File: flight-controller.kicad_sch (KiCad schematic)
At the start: 25 parts, among them CN10 Conn_02x17_Odd_Even, CN7 Conn_02x10_Odd_Even, CN8 Conn_02x08_Odd_Even, CN9 Conn_02x15_Odd_Even, J1 Conn_01x04, J7 J_ESC_POWER, Q1 2N2222

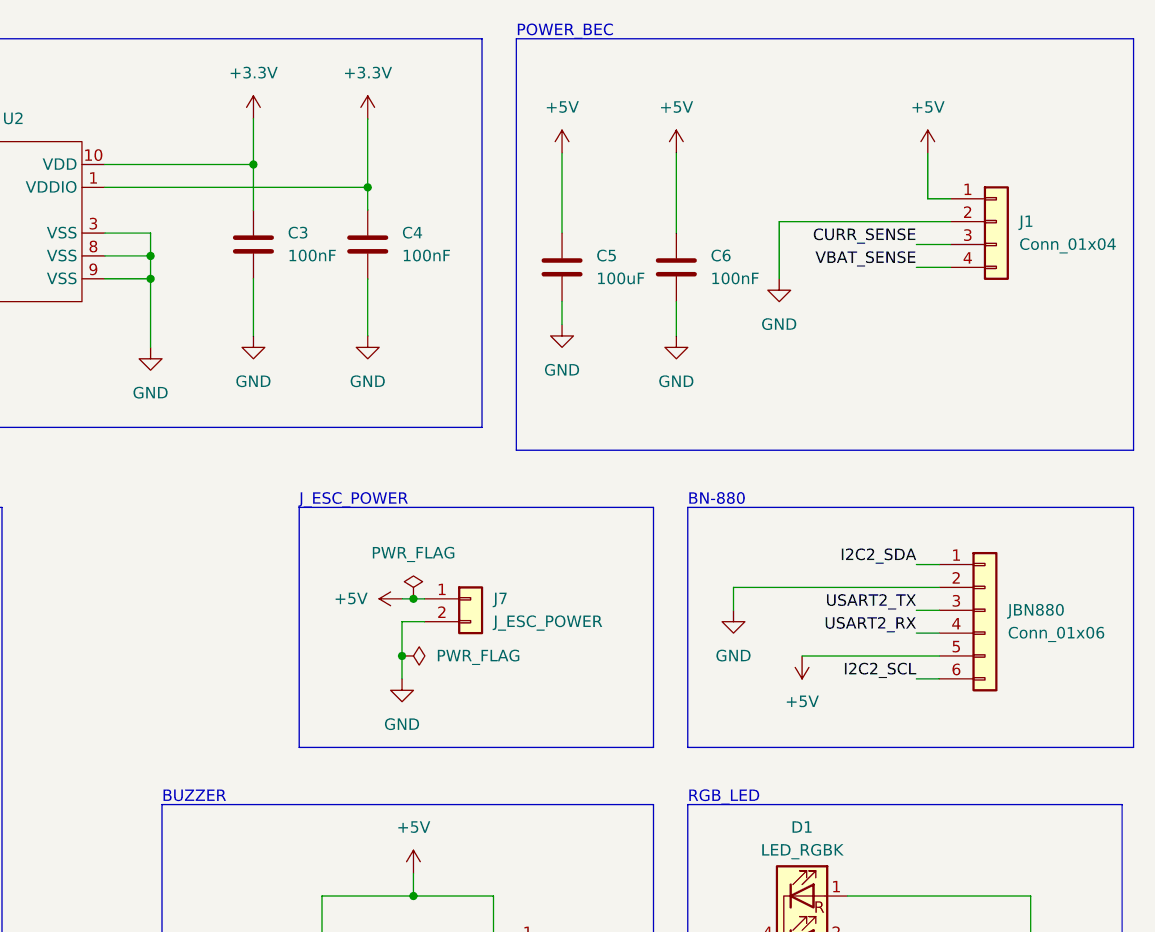
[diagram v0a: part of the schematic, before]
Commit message: feat: Added diodes to power inputs
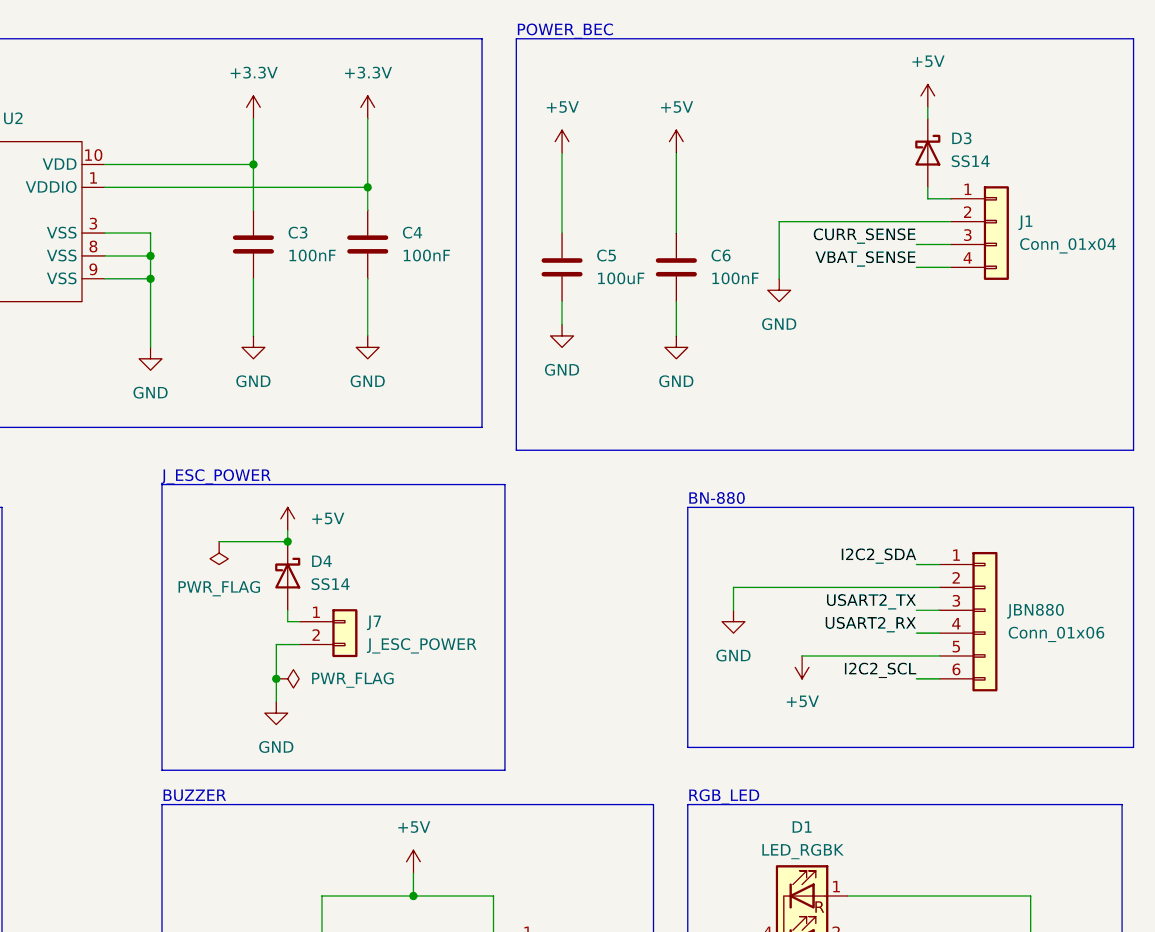
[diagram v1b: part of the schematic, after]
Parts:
- added D3, D4: SS14, symbol Device:D_Schottky
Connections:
- net +5V: now also D3.1 (K), D4.1 (K); no longer J1.1 (Pin_1), J7.1 (Pin_1)
- new net: D4.2 (A), J7.1 (Pin_1)
- new net: D3.2 (A), J1.1 (Pin_1)
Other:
- moved on the sheet: J7

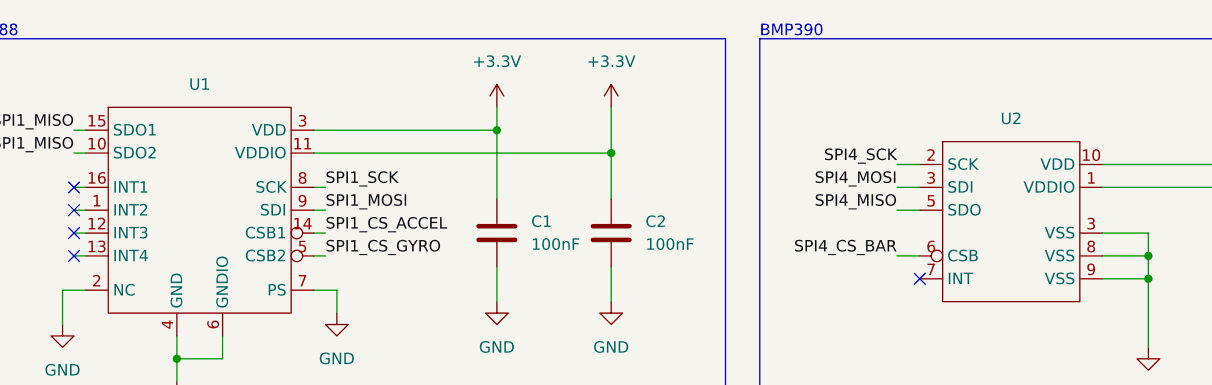
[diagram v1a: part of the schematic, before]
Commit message: fix: Added values to bmi and bmp sensors
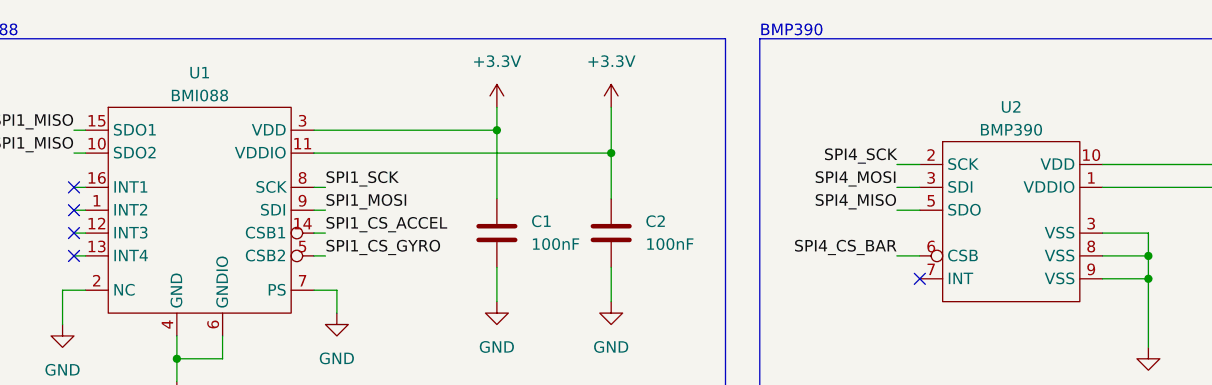
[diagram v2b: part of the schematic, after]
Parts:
- U1: value ~ -> BMI088
- U2: value ~ -> BMP390
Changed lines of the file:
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@@
   )
   (symbol (lib_id "fc_custom:BMI088") (at 48.26 43.18 0) (unit 1)
-    (in_bom yes) (on_board yes) (dnp no) (fields_autoplaced)
-    (property "Reference" "U1" (at 48.26 29.21 0)
-      (effects (font (size 1.27 1.27)))
-    )
-    (property "Value" "~" (at 48.26 43.18 0)
+    (in_bom yes) (on_board yes) (dnp no)
+    (property "Reference" "U1" (at 48.26 27.94 0)
+      (effects (font (size 1.27 1.27)))
+    )
+    (property "Value" "BMI088" (at 48.26 30.48 0)
       (effects (font (size 1.27 1.27)))
     )
@@
   )
   (symbol (lib_id "fc_custom:BMP390") (at 138.43 44.45 0) (unit 1)
-    (in_bom yes) (on_board yes) (dnp no) (fields_autoplaced)
-    (property "Reference" "U2" (at 138.43 33.02 0)
-      (effects (font (size 1.27 1.27)))
-    )
-    (property "Value" "~" (at 138.43 44.45 0)
-      (effects (font (size 1.27 1.27)))
-    )
+    (in_bom yes) (on_board yes) (dnp no)
+    (property "Reference" "U2" (at 138.43 31.75 0)
+      (effects (font (size 1.27 1.27)))
+    )
+    (property "Value" "BMP390" (at 138.43 34.29 0)
+      (effects (font (size 1.27 1.27)))
+    )

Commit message: chore: Added footprints to elements
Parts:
- BZ1: footprint (none) -> Buzzer_Beeper:Buzzer_12x9.5mm_P7.60mm
- C1, C2, C3, C4, C6: footprint (none) -> Capacitor_SMD:C_0402_1005Metric
- C5: footprint (none) -> Capacitor_THT:CP_Radial_D6.3mm_P2.50mm
- CN10: footprint (none) -> Connector_PinHeader_2.54mm:PinHeader_2x17_P2.54mm_Vertical
- CN7: footprint (none) -> Connector_PinHeader_2.54mm:PinHeader_2x10_P2.54mm_Vertical
- CN8: footprint (none) -> Connector_PinHeader_2.54mm:PinHeader_2x08_P2.54mm_Vertical
- CN9: footprint (none) -> Connector_PinHeader_2.54mm:PinHeader_2x15_P2.54mm_Vertical
- D1: footprint (none) -> LED_THT:LED_D5.0mm-4_RGB
- D3, D4: footprint (none) -> Diode_SMD:D_SOD-123
- J1: footprint (none) -> Connector_PinHeader_2.54mm:PinHeader_1x04_P2.54mm_Vertical
- J7: footprint (none) -> Connector_PinHeader_2.54mm:PinHeader_1x02_P2.54mm_Vertical
- JBN880: footprint (none) -> Connector_PinHeader_2.54mm:PinHeader_1x06_P2.54mm_Vertical
- Q1: footprint Package_TO_SOT_THT:TO-39-3 -> Package_TO_SOT_THT:TO-92_Inline
- R1, R2, R3, R4, R5, R6: footprint (none) -> Resistor_SMD:R_0402_1005Metric
- U1: footprint (none) -> fc_library:BMI088
- U2: footprint (none) -> fc_library:BMP390L
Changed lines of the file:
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@@
       (effects (font (size 1.27 1.27)) (justify right))
     )
-    (property "Footprint" "" (at 93.0148 41.91 0)
+    (property "Footprint" "Capacitor_SMD:C_0402_1005Metric" (at 93.0148 41.91 0)
       (effects (font (size 1.27 1.27)) hide)
     )
@@
       (effects (font (size 1.27 1.27)))
     )
-    (property "Footprint" "" (at 63.5 97.79 0)
+    (property "Footprint" "Connector_PinHeader_2.54mm:PinHeader_2x08_P2.54mm_Vertical" (at 63.5 97.79 0)
       (effects (font (size 1.27 1.27)) hide)
     )
@@
       (effects (font (size 1.27 1.27)) (justify left))
     )
-    (property "Footprint" "" (at 242.062 135.89 90)
+    (property "Footprint" "Resistor_SMD:R_0402_1005Metric" (at 242.062 135.89 90)
       (effects (font (size 1.27 1.27)) hide)
     )
@@
       (effects (font (size 1.27 1.27)) (justify left))
     )
-    (property "Footprint" "Package_TO_SOT_THT:TO-39-3" (at 185.42 146.685 0)
+    (property "Footprint" "Package_TO_SOT_THT:TO-92_Inline" (at 185.42 146.685 0)
       (effects (font (size 1.27 1.27) italic) (justify left) hide)
     )
@@
       (effects (font (size 1.27 1.27)))
     )
-    (property "Footprint" "" (at 48.26 43.18 0)
-      (effects (font (size 1.27 1.27)) hide)
-    )
-    (property "Datasheet" "" (at 48.26 43.18 0)
+    (property "Footprint" "fc_library:BMI088" (at 48.26 43.18 0)
+      (effects (font (size 1.27 1.27)) hide)
+    )
+    (property "Datasheet" "https://www.bosch-sensortec.com/media/boschsensortec/downloads/datasheets/bst-bmi088-ds001.pdf" (at 48.26 43.18 0)
       (effects (font (size 1.27 1.27)) hide)
     )
@@
       (effects (font (size 1.27 1.27)) (justify left))
     )
-    (property "Footprint" "" (at 168.91 83.82 0)
+    (property "Footprint" "Diode_SMD:D_SOD-123" (at 168.91 83.82 0)
       (effects (font (size 1.27 1.27)) hide)
     )
@@
       (effects (font (size 1.27 1.27)) (justify left))
     )
-    (property "Footprint" "" (at 40.132 121.92 90)
+    (property "Footprint" "Resistor_SMD:R_0402_1005Metric" (at 40.132 121.92 90)
       (effects (font (size 1.27 1.27)) hide)
     )
@@
       (effects (font (size 1.27 1.27)) (justify left))
     )
-    (property "Footprint" "" (at 35.052 143.51 90)
+    (property "Footprint" "Resistor_SMD:R_0402_1005Metric" (at 35.052 143.51 90)
       (effects (font (size 1.27 1.27)) hide)
     )
@@
       (effects (font (size 1.27 1.27)) (justify left))
     )
-    (property "Footprint" "" (at 246.38 87.63 0)
+    (property "Footprint" "Connector_PinHeader_2.54mm:PinHeader_1x06_P2.54mm_Vertical" (at 246.38 87.63 0)
       (effects (font (size 1.27 1.27)) hide)
     )
@@
       (effects (font (size 1.27 1.27)))
     )
-    (property "Footprint" "" (at 111.76 146.05 0)
+    (property "Footprint" "Connector_PinHeader_2.54mm:PinHeader_2x17_P2.54mm_Vertical" (at 111.76 146.05 0)
       (effects (font (size 1.27 1.27)) hide)
     )
@@
       (effects (font (size 1.27 1.27)) (justify left))
     )
-    (property "Footprint" "" (at 240.03 36.83 0)
+    (property "Footprint" "Diode_SMD:D_SOD-123" (at 240.03 36.83 0)
       (effects (font (size 1.27 1.27)) hide)
     )
@@
       (effects (font (size 1.27 1.27)))
     )
-    (property "Footprint" "" (at 226.06 125.73 0)
+    (property "Footprint" "LED_THT:LED_D5.0mm-4_RGB" (at 226.06 125.73 0)
       (effects (font (size 1.27 1.27)) hide)
     )
@@
       (effects (font (size 1.27 1.27)) (justify left))
     )
-    (property "Footprint" "" (at 200.3552 53.34 0)
+    (property "Footprint" "Capacitor_THT:CP_Radial_D6.3mm_P2.50mm" (at 200.3552 53.34 0)
       (effects (font (size 1.27 1.27)) hide)
     )
@@
       (effects (font (size 1.27 1.27)) (justify left))
     )
-    (property "Footprint" "" (at 247.65 44.45 0)
+    (property "Footprint" "Connector_PinHeader_2.54mm:PinHeader_1x04_P2.54mm_Vertical" (at 247.65 44.45 0)
       (effects (font (size 1.27 1.27)) hide)
     )
@@
       (effects (font (size 1.27 1.27)) (justify left))
     )
-    (property "Footprint" "" (at 82.2452 49.53 0)
+    (property "Footprint" "Capacitor_SMD:C_0402_1005Metric" (at 82.2452 49.53 0)
       (effects (font (size 1.27 1.27)) hide)
     )
@@
       (effects (font (size 1.27 1.27)) (justify left))
     )
-    (property "Footprint" "" (at 213.0552 53.34 0)
+    (property "Footprint" "Capacitor_SMD:C_0402_1005Metric" (at 213.0552 53.34 0)
       (effects (font (size 1.27 1.27)) hide)
     )
@@
       (effects (font (size 1.27 1.27)) (justify left))
     )
-    (property "Footprint" "" (at 234.442 135.89 90)
+    (property "Footprint" "Resistor_SMD:R_0402_1005Metric" (at 234.442 135.89 90)
       (effects (font (size 1.27 1.27)) hide)
     )
@@
       (effects (font (size 1.27 1.27)))
     )
-    (property "Footprint" "" (at 168.91 146.558 90)
+    (property "Footprint" "Resistor_SMD:R_0402_1005Metric" (at 168.91 146.558 90)
       (effects (font (size 1.27 1.27)) hide)
     )
@@
       (effects (font (size 1.27 1.27)) (justify left))
     )
-    (property "Footprint" "" (at 196.215 124.46 90)
+    (property "Footprint" "Buzzer_Beeper:Buzzer_12x9.5mm_P7.60mm" (at 196.215 124.46 90)
       (effects (font (size 1.27 1.27)) hide)
     )
@@
       (effects (font (size 1.27 1.27)) (justify left))
     )
-    (property "Footprint" "" (at 175.26 88.9 0)
+    (property "Footprint" "Connector_PinHeader_2.54mm:PinHeader_1x02_P2.54mm_Vertical" (at 175.26 88.9 0)
       (effects (font (size 1.27 1.27)) hide)
     )
@@
       (effects (font (size 1.27 1.27)) (justify left))
     )
-    (property "Footprint" "" (at 249.682 135.89 90)
+    (property "Footprint" "Resistor_SMD:R_0402_1005Metric" (at 249.682 135.89 90)
       (effects (font (size 1.27 1.27)) hide)
     )
@@
       (effects (font (size 1.27 1.27)) (justify left))
     )
-    (property "Footprint" "" (at 178.7652 50.8 0)
+    (property "Footprint" "Capacitor_SMD:C_0402_1005Metric" (at 178.7652 50.8 0)
       (effects (font (size 1.27 1.27)) hide)
     )
@@
       (effects (font (size 1.27 1.27)))
     )
-    (property "Footprint" "" (at 63.5 142.24 0)
+    (property "Footprint" "Connector_PinHeader_2.54mm:PinHeader_2x15_P2.54mm_Vertical" (at 63.5 142.24 0)
       (effects (font (size 1.27 1.27)) hide)
     )
@@
       (effects (font (size 1.27 1.27)))
     )
-    (property "Footprint" "" (at 138.43 44.45 0)
-      (effects (font (size 1.27 1.27)) hide)
-    )
-    (property "Datasheet" "" (at 138.43 44.45 0)
+    (property "Footprint" "fc_library:BMP390L" (at 138.43 44.45 0)
+      (effects (font (size 1.27 1.27)) hide)
+    )
+    (property "Datasheet" "https://www.bosch-sensortec.com/media/boschsensortec/downloads/datasheets/bst-bmp390-ds002.pdf" (at 138.43 44.45 0)
       (effects (font (size 1.27 1.27)) hide)
     )
@@
       (effects (font (size 1.27 1.27)))
     )
-    (property "Footprint" "" (at 111.76 100.33 0)
+    (property "Footprint" "Connector_PinHeader_2.54mm:PinHeader_2x10_P2.54mm_Vertical" (at 111.76 100.33 0)
       (effects (font (size 1.27 1.27)) hide)
     )
@@
       (effects (font (size 1.27 1.27)) (justify left))
     )
-    (property "Footprint" "" (at 166.0652 50.8 0)
-      (effects (font (size 1.27 1.27)) hide)
-    )
+    (property "Footprint" "Capacitor_SMD:C_0402_1005Metric" (at 166.0652 50.8 0)
+      (effects (font (size 1.27 1.27)) hide)
+    )

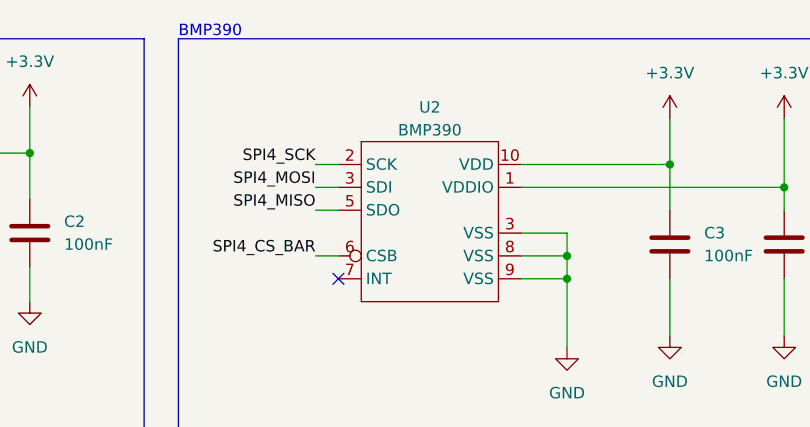
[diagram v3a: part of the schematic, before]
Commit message: fix: Correct pin 4 of bmp390
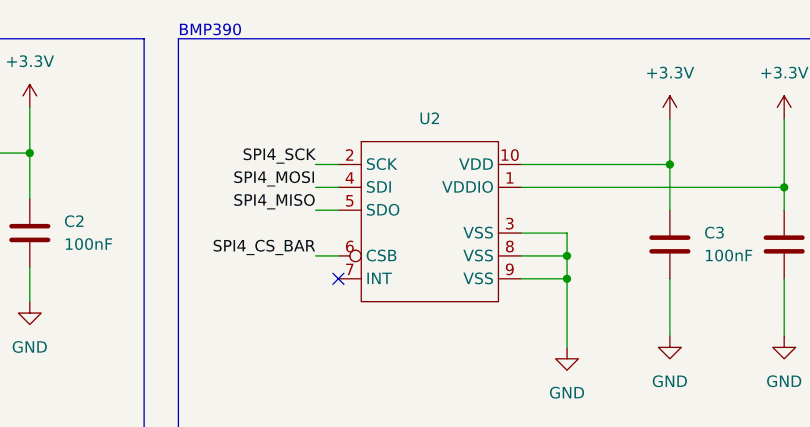
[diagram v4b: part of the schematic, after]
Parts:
- U2: value BMP390 -> ~; footprint fc_library:BMP390L -> (none)
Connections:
- net SPI4_MOSI: now also U2.4 (SDI); no longer U2.3 (VSS)
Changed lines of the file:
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@@
+    )
+  )
+  (symbol (lib_id "fc_custom:BMP390") (at 138.43 44.45 0) (unit 1)
+    (in_bom yes) (on_board yes) (dnp no) (fields_autoplaced)
+    (property "Reference" "U2" (at 138.43 33.02 0)
+      (effects (font (size 1.27 1.27)))
+    )
+    (property "Value" "~" (at 138.43 44.45 0)
+      (effects (font (size 1.27 1.27)))
+    )
+    (property "Footprint" "" (at 138.43 44.45 0)
+      (effects (font (size 1.27 1.27)) hide)
+    )
+    (property "Datasheet" "" (at 138.43 44.45 0)
+      (effects (font (size 1.27 1.27)) hide)
+    )
+    (pin "8")
+    (pin "10")
+    (pin "9")
+    (pin "2")
+    (pin "3")
+    (pin "1")
+    (pin "4")
+    (pin "5")
+    (pin "6")
+    (pin "7")
+    (instances
+      (project "flight-controller"
+        (path "/1e8bc6c3-9c25-4744-8bc3-112c39d50b38"
+          (reference "U2") (unit 1)
+        )
+      )
     )
   )
@@
         )
       )
-    )
-  )
-  (symbol (lib_id "fc_custom:BMP390") (at 138.43 44.45 0) (unit 1)
-    (in_bom yes) (on_board yes) (dnp no)
-    (property "Reference" "U2" (at 138.43 31.75 0)
-      (effects (font (size 1.27 1.27)))
-    )
-    (property "Value" "BMP390" (at 138.43 34.29 0)
-      (effects (font (size 1.27 1.27)))
-    )
-    (property "Footprint" "fc_library:BMP390L" (at 138.43 44.45 0)
-      (effects (font (size 1.27 1.27)) hide)
-    )
-    (property "Datasheet" "https://www.bosch-sensortec.com/media/boschsensortec/downloads/datasheets/bst-bmp390-ds002.pdf" (at 138.43 44.45 0)
-      (effects (font (size 1.27 1.27)) hide)
-    )
-    (pin "7")
-    (pin "10")
-    (pin "3")
-    (pin "2")
-    (pin "3")
-    (pin "5")
-    (pin "6")
-    (pin "8")
-    (pin "9")
-    (pin "1")
-    (instances
-      (project "flight-controller"
-        (path "/1e8bc6c3-9c25-4744-8bc3-112c39d50b38"
-          (reference "U2") (unit 1)
-        )
-      )

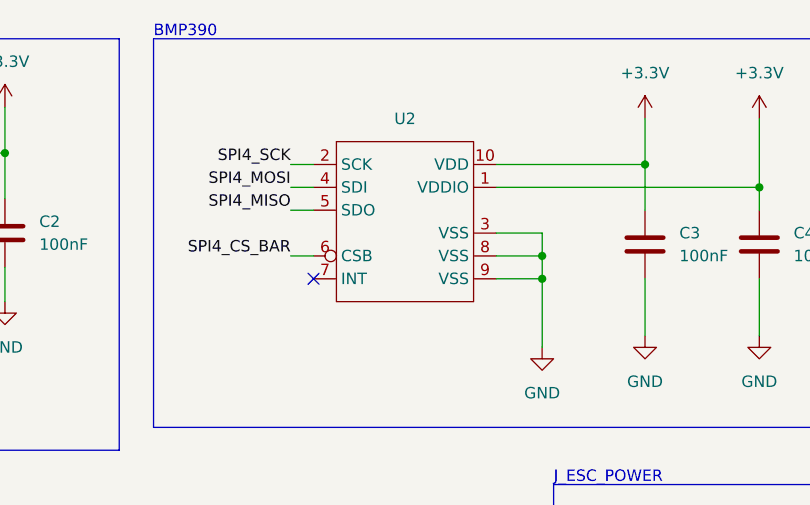
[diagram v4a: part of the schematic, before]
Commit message: fix: Corrected buzzer footprint
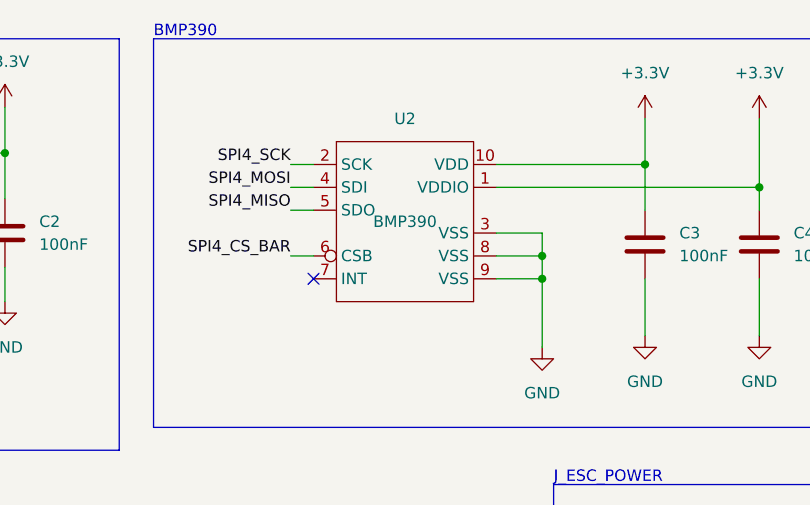
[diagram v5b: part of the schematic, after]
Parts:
- BZ1: footprint Buzzer_Beeper:Buzzer_12x9.5mm_P7.60mm -> Buzzer_Beeper:Buzzer_12x9.5RM7.6
- U2: value ~ -> BMP390; footprint (none) -> fc_library:BMP390L
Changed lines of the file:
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@@
       (effects (font (size 1.27 1.27)))
     )
-    (property "Value" "~" (at 138.43 44.45 0)
+    (property "Value" "BMP390" (at 138.43 44.45 0)
       (effects (font (size 1.27 1.27)))
     )
-    (property "Footprint" "" (at 138.43 44.45 0)
+    (property "Footprint" "fc_library:BMP390L" (at 138.43 44.45 0)
       (effects (font (size 1.27 1.27)) hide)
     )
-    (property "Datasheet" "" (at 138.43 44.45 0)
+    (property "Datasheet" "https://www.bosch-sensortec.com/media/boschsensortec/downloads/datasheets/bst-bmp390-ds002.pdf" (at 138.43 44.45 0)
       (effects (font (size 1.27 1.27)) hide)
     )
@@
       (effects (font (size 1.27 1.27)) (justify left))
     )
-    (property "Footprint" "Buzzer_Beeper:Buzzer_12x9.5mm_P7.60mm" (at 196.215 124.46 90)
+    (property "Footprint" "Buzzer_Beeper:Buzzer_12x9.5RM7.6" (at 196.215 124.46 90)
       (effects (font (size 1.27 1.27)) hide)
     )
